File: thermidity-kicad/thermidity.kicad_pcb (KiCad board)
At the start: 2 copper layers, 60 x 30 mm, 22 parts, among them J1 Battery, J2 Display, J3 ISP, U1 MCP1501-30, U2 ATmega328P, U3 TMP36, U4 HIH-5030

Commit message: trying to finalize...
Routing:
- net GND: track 33.5 -> 34.7 mm, vias 12 -> 13
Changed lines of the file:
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@@
   (gr_rect (start 111.7 58.9) (end 171.7 88.9) (layer "Edge.Cuts") (width 0.1) (fill none))
   (gr_rect (start 111.7 58.9) (end 171.7 88.9) (layer "F.CrtYd") (width 0.05) (fill none))
-  (gr_text "Dode's Thermidity" (at 156.972 64.7192) (layer "User.1")
+  (gr_text "Dode's Thermidity" (at 156.972 64.7192) (layer "F.SilkS")
     (effects (font (size 1.9 1.9) (thickness 0.15)))
   )
-  (gr_text "https://luniks.net/thermidity.jsp" (at 156.972 66.9544) (layer "User.1")
+  (gr_text "https://luniks.net/thermidity.jsp" (at 156.972 66.9544) (layer "F.SilkS")
     (effects (font (size 1 1) (thickness 0.15)))
   )
   (segment (start 135.9916 86.3477) (end 137.8081 86.3477) (width 0.25) (layer "F.Cu") (net 1))
-  (segment (start 139.71 74.9202) (end 140.2654 74.3648) (width 0.25) (layer "F.Cu") (net 1))
   (segment (start 149.6904 75.1648) (end 148.6404 75.1648) (width 0.25) (layer "F.Cu") (net 1))
   (segment (start 147.2852 84.836) (end 145.6944 84.836) (width 0.25) (layer "F.Cu") (net 1))
+  (segment (start 139.6048 74.3648) (end 139.5984 74.3712) (width 0.25) (layer "F.Cu") (net 1))
   (segment (start 123.377751 81.0514) (end 123.001 81.0514) (width 0.25) (layer "F.Cu") (net 1))
+  (segment (start 141.1904 74.3648) (end 139.6048 74.3648) (width 0.25) (layer "F.Cu") (net 1))
   (segment (start 131.7244 86.3477) (end 133.4131 86.3477) (width 0.25) (layer "F.Cu") (net 1))
-  (segment (start 140.2654 74.3648) (end 141.1904 74.3648) (width 0.25) (layer "F.Cu") (net 1))
   (segment (start 148.6404 75.1648) (end 148.5654 75.0898) (width 0.25) (layer "F.Cu") (net 1))
   (segment (start 153.1142 83.566) (end 151.2316 83.566) (width 0.25) (layer "F.Cu") (net 1))
   (segment (start 134.137 63.3472) (end 134.137 65.253) (width 0.25) (layer "F.Cu") (net 1))
   (segment (start 148.6948 73.5648) (end 149.6904 73.5648) (width 0.25) (layer "F.Cu") (net 1))
+  (segment (start 118.5724 70.922) (end 118.5672 70.9168) (width 0.25) (layer "F.Cu") (net 1))
   (segment (start 123.001 78.5114) (end 123.377751 78.5114) (width 0.25) (layer "F.Cu") (net 1))
   (segment (start 136.0076 77.3684) (end 137.3966 75.9794) (width 0.25) (layer "F.Cu") (net 1))
@@
   (segment (start 134.7847 69.6976) (end 133.2992 69.6976) (width 0.25) (layer "F.Cu") (net 1))
   (segment (start 148.5654 75.0898) (end 148.5654 73.6942) (width 0.25) (layer "F.Cu") (net 1))
+  (segment (start 119.904 70.922) (end 118.5724 70.922) (width 0.25) (layer "F.Cu") (net 1))
   (segment (start 149.6904 75.1648) (end 153.1043 75.1648) (width 0.25) (layer "F.Cu") (net 1))
   (segment (start 153.1043 75.1648) (end 153.416 75.4765) (width 0.25) (layer "F.Cu") (net 1))
@@
   (segment (start 119.904 70.922) (end 119.904 73.7616) (width 0.25) (layer "F.Cu") (net 1))
   (via (at 145.8976 84.836) (size 0.8) (drill 0.4) (layers "F.Cu" "B.Cu") (net 1))
+  (via (at 139.5984 74.3712) (size 0.8) (drill 0.4) (layers "F.Cu" "B.Cu") (free) (net 1))
   (via (at 125.476 81.026) (size 0.8) (drill 0.4) (layers "F.Cu" "B.Cu") (free) (net 1))
-  (via (at 139.71 74.9202) (size 0.8) (drill 0.4) (layers "F.Cu" "B.Cu") (net 1))
   (via (at 133.4131 86.3477) (size 0.8) (drill 0.4) (layers "F.Cu" "B.Cu") (net 1))
+  (via (at 118.5672 70.9168) (size 0.8) (drill 0.4) (layers "F.Cu" "B.Cu") (free) (net 1))
   (via (at 133.2992 73.66) (size 0.8) (drill 0.4) (layers "F.Cu" "B.Cu") (net 1))
   (via (at 153.416 76.9112) (size 0.8) (drill 0.4) (layers "F.Cu" "B.Cu") (net 1))

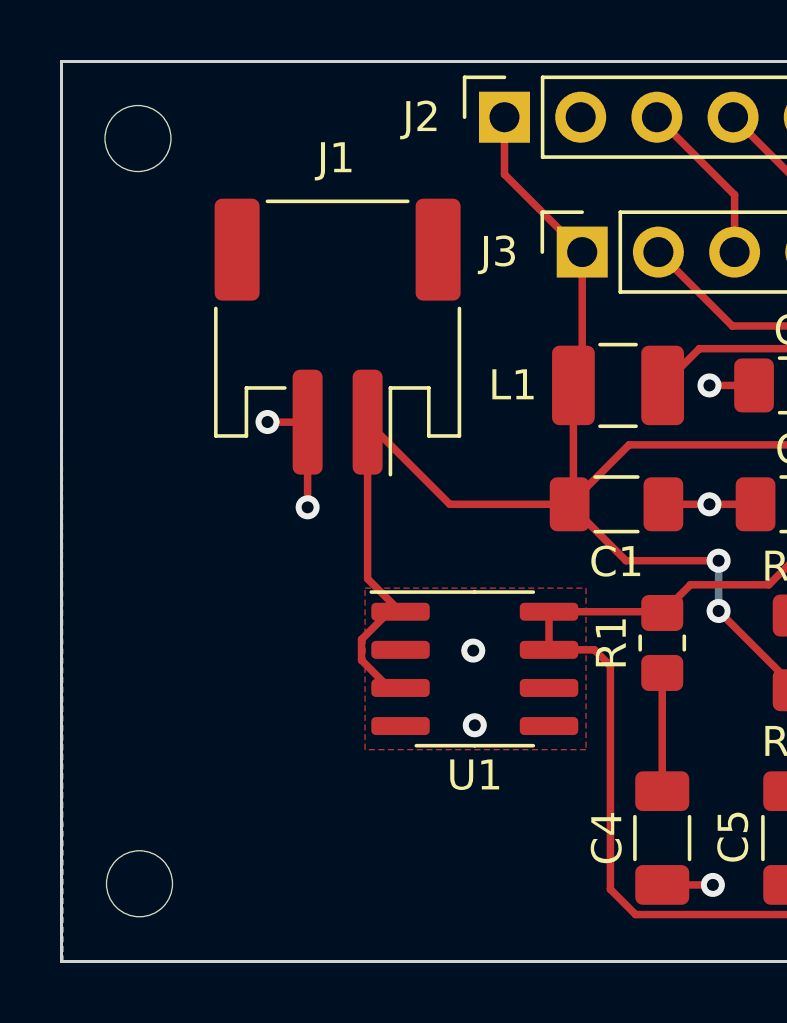
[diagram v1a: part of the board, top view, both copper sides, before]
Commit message: put back ground area and add vias for better connection
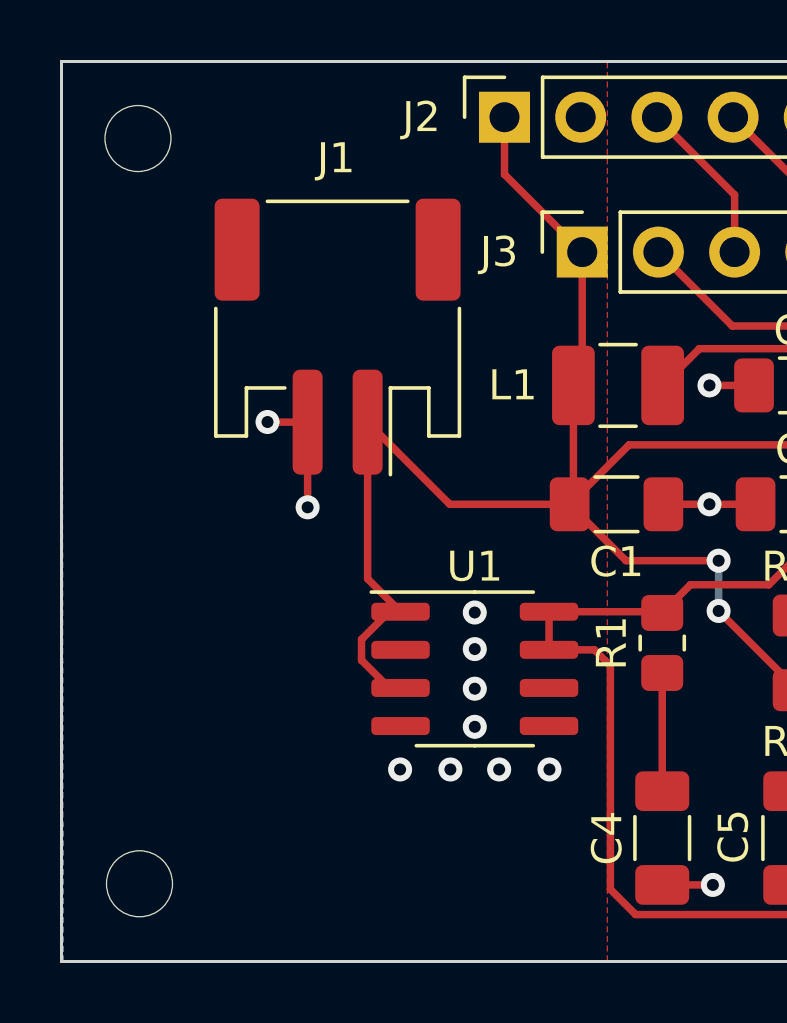
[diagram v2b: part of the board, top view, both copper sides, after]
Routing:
- net GND: vias 13 -> 19
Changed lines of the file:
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@@
     (property "Sheetname" "")
     (attr smd)
-    (fp_text reference "U1" (at 0 3.556) (layer "F.SilkS")
+    (fp_text reference "U1" (at 0 -3.4036) (layer "F.SilkS")
       (effects (font (size 1 1) (thickness 0.15)))
     )
@@
   (segment (start 119.904 70.922) (end 119.904 73.7616) (width 0.25) (layer "F.Cu") (net 1))
   (via (at 145.8976 84.836) (size 0.8) (drill 0.4) (layers "F.Cu" "B.Cu") (net 1))
+  (via (at 125.476 77.2668) (size 0.8) (drill 0.4) (layers "F.Cu" "B.Cu") (free) (net 1))
   (via (at 139.5984 74.3712) (size 0.8) (drill 0.4) (layers "F.Cu" "B.Cu") (free) (net 1))
-  (via (at 125.476 81.026) (size 0.8) (drill 0.4) (layers "F.Cu" "B.Cu") (free) (net 1))
+  (via (at 125.476 81.0768) (size 0.8) (drill 0.4) (layers "F.Cu" "B.Cu") (free) (net 1))
   (via (at 133.4131 86.3477) (size 0.8) (drill 0.4) (layers "F.Cu" "B.Cu") (net 1))
   (via (at 118.5672 70.9168) (size 0.8) (drill 0.4) (layers "F.Cu" "B.Cu") (free) (net 1))
   (via (at 133.2992 73.66) (size 0.8) (drill 0.4) (layers "F.Cu" "B.Cu") (net 1))
+  (via (at 122.9868 82.4992) (size 0.8) (drill 0.4) (layers "F.Cu" "B.Cu") (free) (net 1))
   (via (at 153.416 76.9112) (size 0.8) (drill 0.4) (layers "F.Cu" "B.Cu") (net 1))
   (via (at 137.668 86.3477) (size 0.8) (drill 0.4) (layers "F.Cu" "B.Cu") (net 1))
-  (via (at 125.4252 78.5368) (size 0.8) (drill 0.4) (layers "F.Cu" "B.Cu") (free) (net 1))
+  (via (at 125.476 78.486) (size 0.8) (drill 0.4) (layers "F.Cu" "B.Cu") (free) (net 1))
+  (via (at 126.2888 82.4992) (size 0.8) (drill 0.4) (layers "F.Cu" "B.Cu") (free) (net 1))
+  (via (at 125.476 79.8068) (size 0.8) (drill 0.4) (layers "F.Cu" "B.Cu") (free) (net 1))
   (via (at 133.2992 69.6976) (size 0.8) (drill 0.4) (layers "F.Cu" "B.Cu") (net 1))
   (via (at 151.384 83.566) (size 0.8) (drill 0.4) (layers "F.Cu" "B.Cu") (net 1))
   (via (at 137.3966 75.9794) (size 0.8) (drill 0.4) (layers "F.Cu" "B.Cu") (net 1))
+  (via (at 127.9652 82.4992) (size 0.8) (drill 0.4) (layers "F.Cu" "B.Cu") (free) (net 1))
+  (via (at 124.6632 82.4992) (size 0.8) (drill 0.4) (layers "F.Cu" "B.Cu") (free) (net 1))
   (via (at 119.904 73.7616) (size 0.8) (drill 0.4) (layers "F.Cu" "B.Cu") (net 1))
   (segment (start 121.701 78.858151) (end 122.624249 79.7814) (width 0.25) (layer "F.Cu") (net 2))
@@
     (polygon
       (pts
-        (xy 129.1844 81.8388)
-        (xy 121.8184 81.8388)
-        (xy 121.8184 76.454)
-        (xy 129.1844 76.454)
+        (xy 129.8956 88.9)
+        (xy 111.7092 88.9)
+        (xy 111.7092 58.928)
+        (xy 129.8956 58.928)
       )
     )

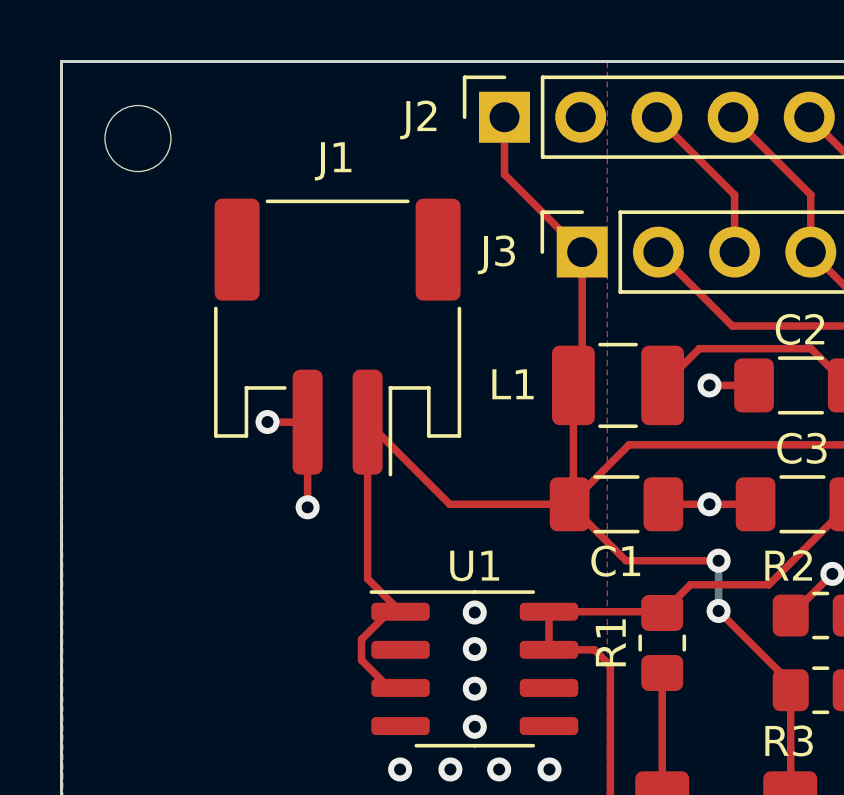
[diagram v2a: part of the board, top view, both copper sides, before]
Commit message: use print instead of SMD for JST connector
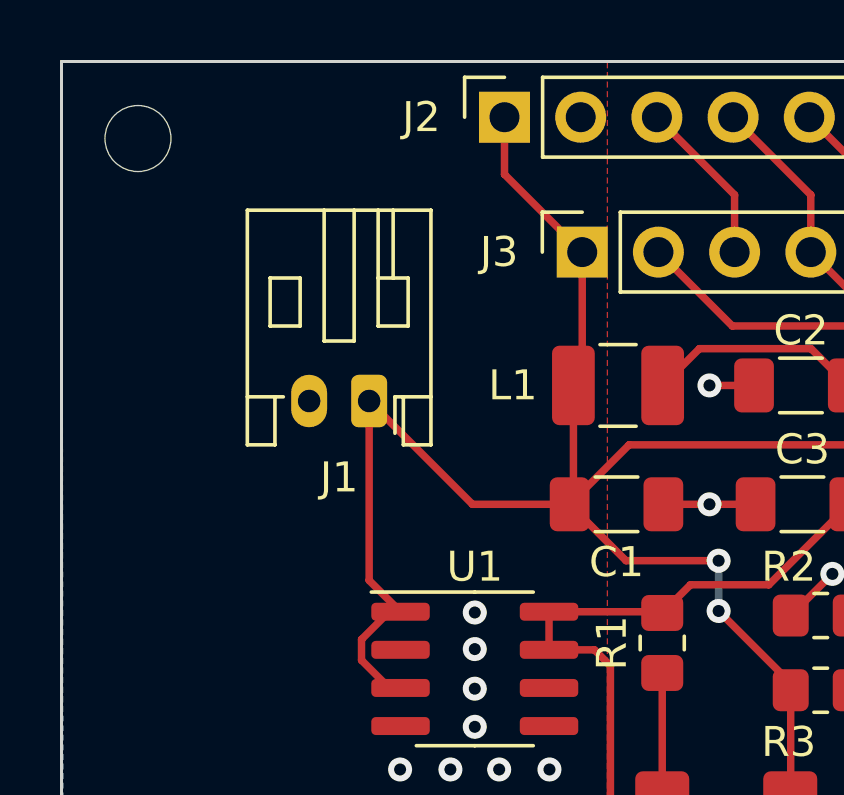
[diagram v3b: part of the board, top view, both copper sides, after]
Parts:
- J1: footprint Connector_JST:JST_PH_S2B-PH-SM4-TB_1x02-1MP_P2.00mm_Horizontal -> Connector_JST:JST_PH_S2B-PH-K_1x02_P2.00mm_Horizontal
- moved J1 2.39 mm to (122.0, 70.2)
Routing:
- net GND: track 34.7 -> 30.5 mm, vias 19 -> 17
- net +BATT: track 81.8 -> 82.7 mm

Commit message: power off vref during idle time reducing consumption from 400uA to 43uA
- power off vref including humidity sensor
- add serial resistor to reduce charge current
- fix pin initialization
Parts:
- added R1: 68, Resistor_SMD:R_0805_2012Metric_Pad1.20x1.40mm_HandSolder, F.Cu at (124.4, 73.7)
- R2: renamed from R1; value 50 -> 51
- moved R3 2.44 mm to (135.1, 78.3), turned to -90 degrees
- moved R4 1.11 mm to (137.6, 78.3), turned to 90 degrees
- moved J1 0.62 mm to (121.6, 69.7)
- renumbered R2 to R4, R4 to R5
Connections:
- C1 pad 2: +BATT -> Net-(C1-Pad2)
- U1 pad 1: +BATT -> Net-(U2-Pad23)
- U1 pad 3: +BATT -> Net-(U2-Pad23)
- U2 pad 23: unconnected-(U2-Pad23) -> Net-(U2-Pad23)
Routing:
- net Net-(U2-Pad23): track 0.00 -> 26.8 mm, vias 0 -> 2
- net GND: track 30.5 -> 24.6 mm, vias 17 -> 13
- net Net-(C1-Pad2): track 0.00 -> 3.23 mm
- net +BATT: track 82.7 -> 85.2 mm
- net Net-(U2-Pad24): track 5.92 -> 7.11 mm
